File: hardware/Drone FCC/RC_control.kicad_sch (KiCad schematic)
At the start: 2 parts, among them J17 DSM Spektrum JST, J18 PPM Dupont

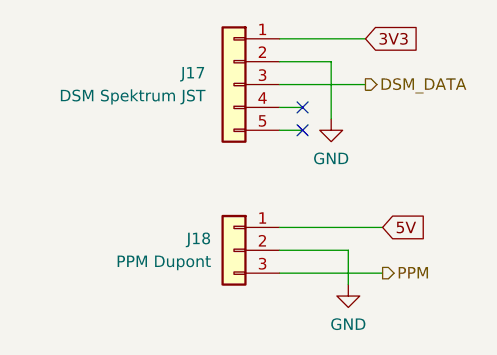
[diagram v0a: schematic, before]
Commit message: moved NRST cap near mcu pin, changed v meas adc pin
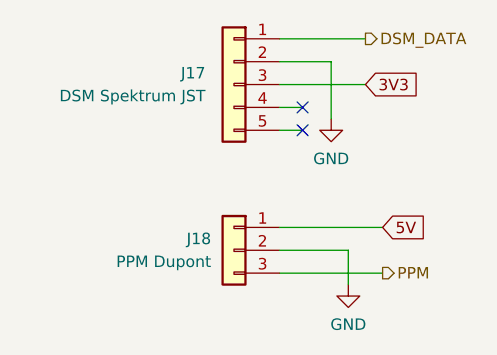
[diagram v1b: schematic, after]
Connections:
- net 3V3: now also J17.3 (Pin_3); no longer J17.1 (Pin_1)
- net DSM_DATA: now also J17.1 (Pin_1); no longer J17.3 (Pin_3)
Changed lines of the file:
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@@
     (stroke (width 0) (type default) (color 0 0 0 0))
   )
-  (wire (pts (xy 151.13 74.295) (xy 160.655 74.295))
+  (wire (pts (xy 151.13 69.215) (xy 160.655 69.215))
     (stroke (width 0) (type default) (color 0 0 0 0))
   )
@@
     (stroke (width 0) (type default) (color 0 0 0 0))
   )
-  (wire (pts (xy 151.13 69.215) (xy 160.655 69.215))
+  (wire (pts (xy 151.13 74.295) (xy 160.655 74.295))
     (stroke (width 0) (type default) (color 0 0 0 0))
   )
@@
     (stroke (width 0) (type default) (color 0 0 0 0))
   )
-  (global_label "3V3" (shape input) (at 160.655 69.215 0) (fields_autoplaced)
+  (global_label "3V3" (shape input) (at 160.655 74.295 0) (fields_autoplaced)
     (effects (font (size 1.27 1.27)) (justify left))
-    (property "Intersheet References" "${INTERSHEET_REFS}" (id 0) (at 166.5757 69.1356 0)
+    (property "Intersheet References" "${INTERSHEET_REFS}" (id 0) (at 166.5757 74.2156 0)
       (effects (font (size 1.27 1.27)) (justify left) hide)
     )
@@
     (effects (font (size 1.27 1.27)) (justify left))
   )
-  (hierarchical_label "DSM_DATA" (shape output) (at 160.655 74.295 0)
+  (hierarchical_label "DSM_DATA" (shape output) (at 160.655 69.215 0)
     (effects (font (size 1.27 1.27)) (justify left))
   )
